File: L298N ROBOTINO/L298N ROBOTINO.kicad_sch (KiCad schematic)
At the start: 40 parts, among them U2 L298N, U4 ESP32-DevKitC, U5 NRF24L01_Breakout, U6 L298N

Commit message: New PCB ver 2 Edit
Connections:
- net CSN: now also U4.27 (GPIO16); no longer U4.29 (GPIO5)
- net at U5.3 (CE): now also U4.28 (GPIO17), U5.8 (IRQ); no longer U4.26 (ADC2_CH0/GPIO4)
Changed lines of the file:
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@@
+	)
+	(junction
+		(at 120.65 119.38)
+		(diameter 0)
+		(color 0 0 0 0)
 	)
 	(junction
@@
 	(wire
 		(pts
-			(xy 107.95 116.84) (xy 120.65 116.84)
-		)
-		(stroke
-			(width 0)
-			(type default)
-		)
-	)
-	(wire
-		(pts
 			(xy 101.6 67.31) (xy 107.95 67.31)
 		)
@@
 	(wire
 		(pts
+			(xy 120.65 116.84) (xy 120.65 119.38)
+		)
+		(stroke
+			(width 0)
+			(type default)
+		)
+	)
+	(wire
+		(pts
 			(xy 62.23 74.93) (xy 68.58 74.93)
 		)
@@
 	(wire
 		(pts
+			(xy 120.65 152.4) (xy 92.71 152.4)
+		)
+		(stroke
+			(width 0)
+			(type default)
+		)
+	)
+	(wire
+		(pts
 			(xy 95.25 67.31) (xy 101.6 67.31)
 		)
@@
 	(wire
 		(pts
-			(xy 92.71 104.14) (xy 107.95 104.14)
-		)
-		(stroke
-			(width 0)
-			(type default)
-		)
-	)
-	(wire
-		(pts
 			(xy 27.94 36.83) (xy 27.94 45.72)
 		)
@@
 	(wire
 		(pts
-			(xy 107.95 104.14) (xy 107.95 116.84)
-		)
-		(stroke
-			(width 0)
-			(type default)
-		)
-	)
-	(wire
-		(pts
 			(xy 209.55 106.68) (xy 209.55 121.92)
 		)
@@
 		(pts
 			(xy 68.58 36.83) (xy 71.12 36.83)
+		)
+		(stroke
+			(width 0)
+			(type default)
+		)
+	)
+	(wire
+		(pts
+			(xy 120.65 119.38) (xy 120.65 152.4)
 		)
 		(stroke
@@
 	(global_label "CSN"
 		(shape input)
-		(at 92.71 106.68 0)
+		(at 92.71 149.86 0)
 		(fields_autoplaced yes)
 		(effects
@@
 		)
 		(property "Intersheetrefs" "${INTERSHEET_REFS}"
-			(at 98.851 106.68 0)
-			(hide yes)
-			(show_name no)
+			(at 98.851 149.86 0)
+			(hide yes)
+			(show_name no)

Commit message: PCB CHO BOARD HAN
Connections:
- net CE: now reaches U4.28 (GPIO17), U5.3 (CE)
- net CE: no longer U5.8 (IRQ)
- net EnA_L: now reaches U4.5 (VDET_1/GPIO34/ADC1_CH6)
- net EnA_L: now also U2.6 (EnA)
- net EnB_L: now reaches U4.6 (VDET_2/GPIO35/ADC1_CH7)
- net EnB_L: now also U2.11 (EnB)
- net EnA renamed EnA_R
- net EnA_R: no longer U2.6 (EnA)
- net EnB renamed EnB_R
- net EnB_R: no longer U2.11 (EnB)
- net MOSI: no longer names the net of U5.6 (MOSI)
- net MOSI: no longer U4.37 (GPIO23)
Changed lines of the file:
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@@
-	)
-	(junction
-		(at 120.65 119.38)
-		(diameter 0)
-		(color 0 0 0 0)
 	)
 	(junction
@@
 	(wire
 		(pts
-			(xy 120.65 116.84) (xy 120.65 119.38)
-		)
-		(stroke
-			(width 0)
-			(type default)
-		)
-	)
-	(wire
-		(pts
 			(xy 62.23 74.93) (xy 68.58 74.93)
 		)
@@
 	(wire
 		(pts
-			(xy 120.65 152.4) (xy 92.71 152.4)
-		)
-		(stroke
-			(width 0)
-			(type default)
-		)
-	)
-	(wire
-		(pts
 			(xy 95.25 67.31) (xy 101.6 67.31)
 		)
@@
 		(pts
 			(xy 68.58 36.83) (xy 71.12 36.83)
-		)
-		(stroke
-			(width 0)
-			(type default)
-		)
-	)
-	(wire
-		(pts
-			(xy 120.65 119.38) (xy 120.65 152.4)
 		)
 		(stroke
@@
 		)
 	)
+	(global_label "CE"
+		(shape input)
+		(at 92.71 152.4 0)
+		(fields_autoplaced yes)
+		(effects
+			(font
+				(size 1.27 1.27)
+			)
+			(justify left)
+		)
+		(property "Intersheetrefs" "${INTERSHEET_REFS}"
+			(at 97.46 152.4 0)
+			(hide yes)
+			(show_name no)
+			(do_not_autoplace no)
+			(effects
+				(font
+					(size 1.27 1.27)
+				)
+				(justify left)
+			)
+		)
+	)
 	(global_label "IN2"
 		(shape output)
@@
 		)
 	)
+	(global_label "EnB_L"
+		(shape input)
+		(at 26.67 119.38 180)
+		(fields_autoplaced yes)
+		(effects
+			(font
+				(size 1.27 1.27)
+			)
+			(justify right)
+		)
+		(property "Intersheetrefs" "${INTERSHEET_REFS}"
+			(at 18.7753 119.38 0)
+			(hide yes)
+			(show_name no)
+			(do_not_autoplace no)
+			(effects
+				(font
+					(size 1.27 1.27)
+				)
+				(justify right)
+			)
+		)
+	)
 	(global_label "IN1"
 		(shape output)
@@
 		)
 	)
-	(global_label "MOSI"
-		(shape output)
-		(at 120.65 104.14 180)
-		(fields_autoplaced yes)
-		(effects
-			(font
-				(size 1.27 1.27)
-			)
-			(justify right)
-		)
-		(property "Intersheetrefs" "${INTERSHEET_REFS}"
-			(at 113.0686 104.14 0)
-			(hide yes)
-			(show_name no)
-			(do_not_autoplace no)
-			(effects
-				(font
-					(size 1.27 1.27)
-				)
-				(justify right)
-			)
-		)
-	)
-	(global_label "EnA"
+	(global_label "EnA_R"
 		(shape input)
 		(at 26.67 99.06 180)
@@
 		)
 		(property "Intersheetrefs" "${INTERSHEET_REFS}"
-			(at 20.9524 99.06 0)
+			(at 18.7148 99.06 0)
 			(hide yes)
 			(show_name no)
@@
 		)
 	)
-	(global_label "EnB"
+	(global_label "EnA_L"
+		(shape input)
+		(at 26.67 116.84 180)
+		(fields_autoplaced yes)
+		(effects
+			(font
+				(size 1.27 1.27)
+			)
+			(justify right)
+		)
+		(property "Intersheetrefs" "${INTERSHEET_REFS}"
+			(at 18.9567 116.84 0)
+			(hide yes)
+			(show_name no)
+			(do_not_autoplace no)
+			(effects
+				(font
+					(size 1.27 1.27)
+				)
+				(justify right)
+			)
+		)
+	)
+	(global_label "EnB_R"
 		(shape input)
 		(at 26.67 96.52 180)
@@
 		)
 		(property "Intersheetrefs" "${INTERSHEET_REFS}"
-			(at 20.771 96.52 0)
+			(at 18.5334 96.52 0)
 			(hide yes)
 			(show_name no)
@@
 		)
 	)
-	(global_label "EnA"
+	(global_label "EnA_R"
 		(shape output)
 		(at 175.26 43.18 180)
@@
 		)
 		(property "Intersheetrefs" "${INTERSHEET_REFS}"
-			(at 169.13 43.18 0)
+			(at 167.3048 43.18 0)
 			(hide yes)
 			(show_name no)
@@
 		)
 	)
-	(global_label "EnA"
+	(global_label "EnA_L"
 		(shape output)
 		(at 175.26 104.14 180)
@@
 		)
 		(property "Intersheetrefs" "${INTERSHEET_REFS}"
-			(at 169.13 104.14 0)
+			(at 167.5467 104.14 0)
 			(hide yes)
 			(show_name no)
@@
 		)
 	)
-	(global_label "EnB"
+	(global_label "EnB_R"
 		(shape output)
 		(at 175.26 53.34 180)
@@
 		)
 		(property "Intersheetrefs" "${INTERSHEET_REFS}"
-			(at 168.7068 53.34 0)
+			(at 167.1234 53.34 0)
 			(hide yes)
 			(show_name no)
@@
 		)
 	)
+	(global_label "CE"
+		(shape output)
+		(at 120.65 116.84 180)
+		(fields_autoplaced yes)
+		(effects
+			(font
+				(size 1.27 1.27)
+			)
+			(justify right)
+		)
+		(property "Intersheetrefs" "${INTERSHEET_REFS}"
+			(at 115.9 116.84 0)
+			(hide yes)
+			(show_name no)
+			(do_not_autoplace no)
+			(effects
+				(font
+					(size 1.27 1.27)
+				)
+				(justify right)
+			)
+		)
+	)
 	(global_label "IN1"
 		(shape input)
@@
 		)
 	)
-	(global_label "MOSI"
-		(shape input)
-		(at 92.71 119.38 0)
-		(fields_autoplaced yes)
-		(effects
-			(font
-				(size 1.27 1.27)
-			)
-			(justify left)
-		)
-		(property "Intersheetrefs" "${INTERSHEET_REFS}"
-			(at 99.6372 119.38 0)
-			(hide yes)
-			(show_name no)
-			(do_not_autoplace no)
-			(effects
-				(font
-					(size 1.27 1.27)
-				)
-				(justify left)
-			)
-		)
-	)
-	(global_label "EnB"
+	(global_label "EnB_L"
 		(shape output)
 		(at 175.26 114.3 180)
@@
 		)
 		(property "Intersheetrefs" "${INTERSHEET_REFS}"
-			(at 168.7068 114.3 0)
-			(hide yes)
-			(show_name no)
+			(at 167.3653 114.3 0)
+			(hide yes)
+			(show_name no)

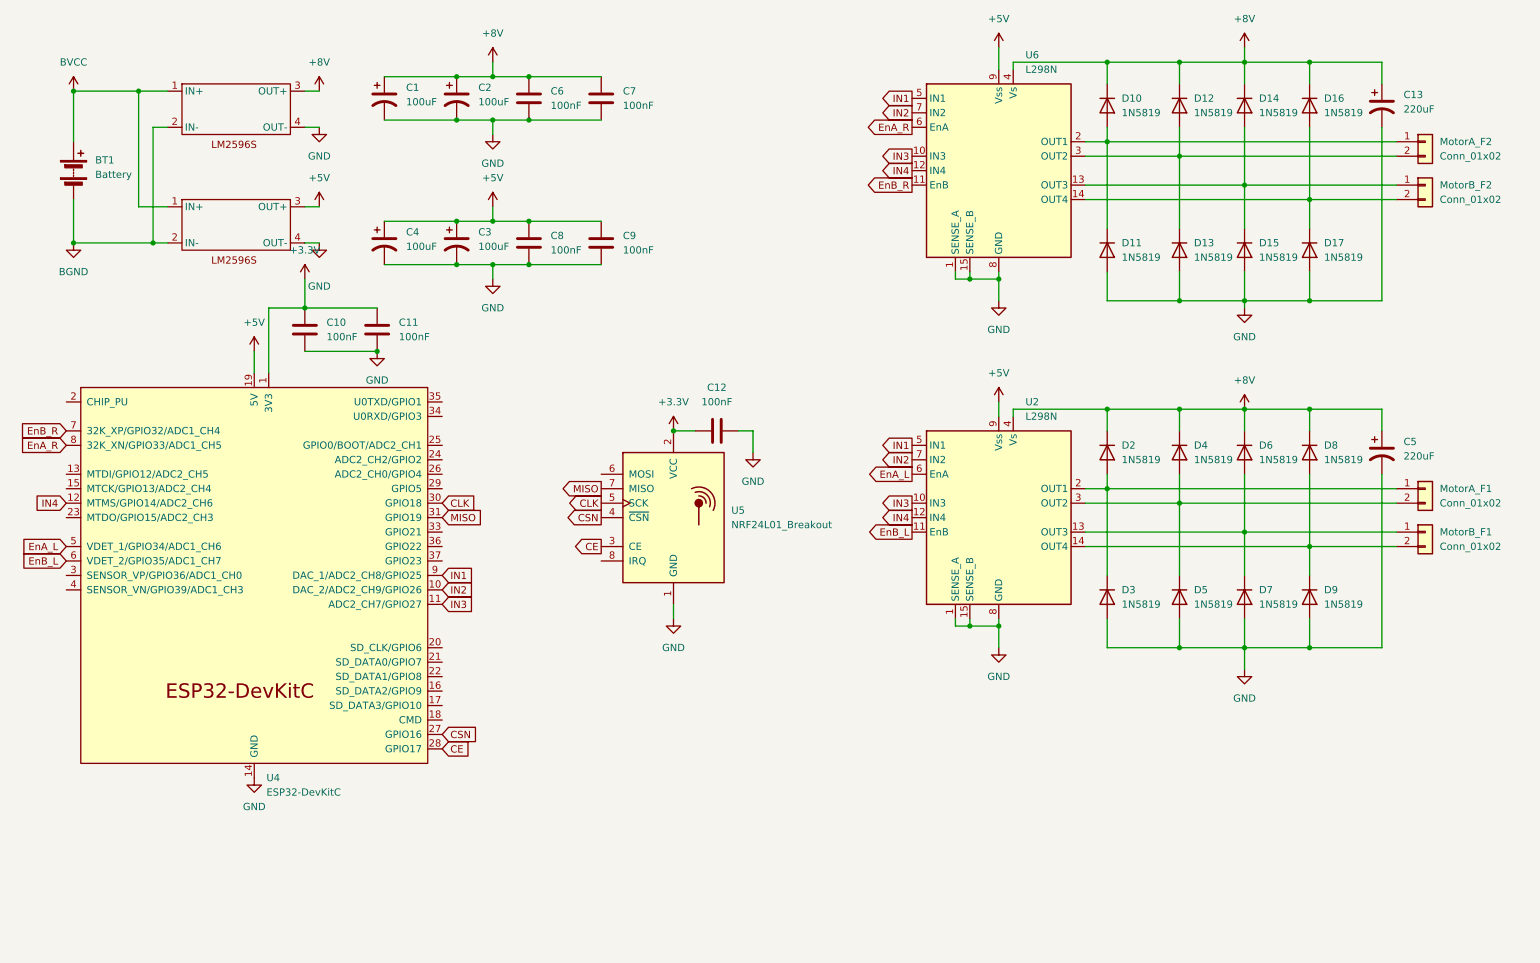
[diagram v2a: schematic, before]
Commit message: Finished L298N PCB, added a 74hc14 to reduce gpios required, changed PCB to 4 layers to add extra wiring, fixed footprints, fixed pin labels
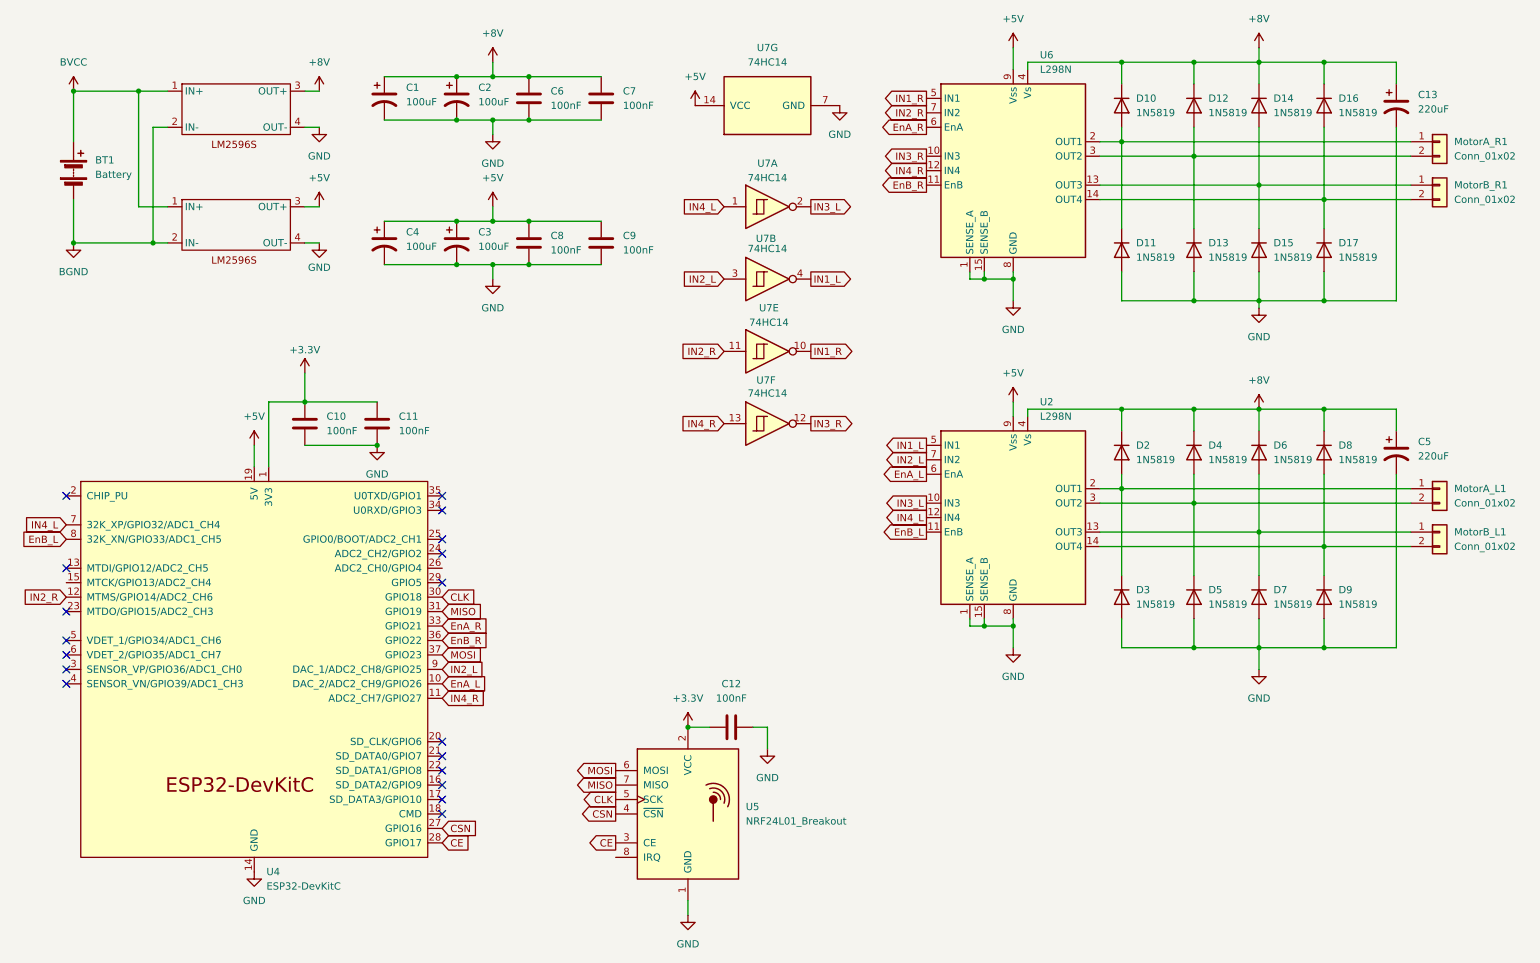
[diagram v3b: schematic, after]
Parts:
- added U7: 74HC14, Package_DIP:DIP-14_W7.62mm, symbol 74xx:74HC14
- U1, U3: footprint ROBOTINO:LM2596S_Module -> LM2596S:LM2596S_Module
- renumbered MotorA_F1 to MotorA_L1, MotorA_F2 to MotorA_R1, MotorB_F1 to MotorB_L1, MotorB_F2 to MotorB_R1
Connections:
- net +5V: now also U7.14 (VCC)
- net EnA_L: now also U4.10 (DAC_2/ADC2_CH9/GPIO26); no longer U4.5 (VDET_1/GPIO34/ADC1_CH6)
- net EnA_R: now also U4.33 (GPIO21); no longer U4.8 (32K_XN/GPIO33/ADC1_CH5)
- net EnB_L: now also U4.8 (32K_XN/GPIO33/ADC1_CH5); no longer U4.6 (VDET_2/GPIO35/ADC1_CH7)
- net EnB_R: now also U4.36 (GPIO22); no longer U4.7 (32K_XP/GPIO32/ADC1_CH4)
- net GND: now also U7.7 (GND)
- net MOSI: now reaches U5.6 (MOSI)
- net MOSI: now also U4.37 (GPIO23)
- removed net IN1: U2.5 (IN1), U4.9 (DAC_1/ADC2_CH8/GPIO25), U6.5 (IN1)
- removed net IN2: U2.7 (IN2), U4.10 (DAC_2/ADC2_CH9/GPIO26), U6.7 (IN2)
- removed net IN3: U2.10 (IN3), U4.11 (ADC2_CH7/GPIO27), U6.10 (IN3)
- removed net IN4: U2.12 (IN4), U4.12 (MTMS/GPIO14/ADC2_CH6), U6.12 (IN4)
- new net IN1_L: U2.5 (IN1), U7.4
- new net IN1_R: U6.5 (IN1), U7.10
- new net IN2_L: U2.7 (IN2), U4.9 (DAC_1/ADC2_CH8/GPIO25), U7.3
- new net IN2_R: U4.12 (MTMS/GPIO14/ADC2_CH6), U6.7 (IN2), U7.11
- new net IN3_L: U2.10 (IN3), U7.2
- new net IN3_R: U6.10 (IN3), U7.12
- new net IN4_L: U2.12 (IN4), U4.7 (32K_XP/GPIO32/ADC1_CH4), U7.1
- new net IN4_R: U4.11 (ADC2_CH7/GPIO27), U6.12 (IN4), U7.13
- no-connect marks 0 -> 18
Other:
- moved on the sheet: C10, C11, C12, C13, C5, D10, D11, D12, D13, D14, D15, D16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
